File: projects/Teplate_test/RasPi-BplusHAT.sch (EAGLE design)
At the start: 1 part, among them K1 PIN20X2

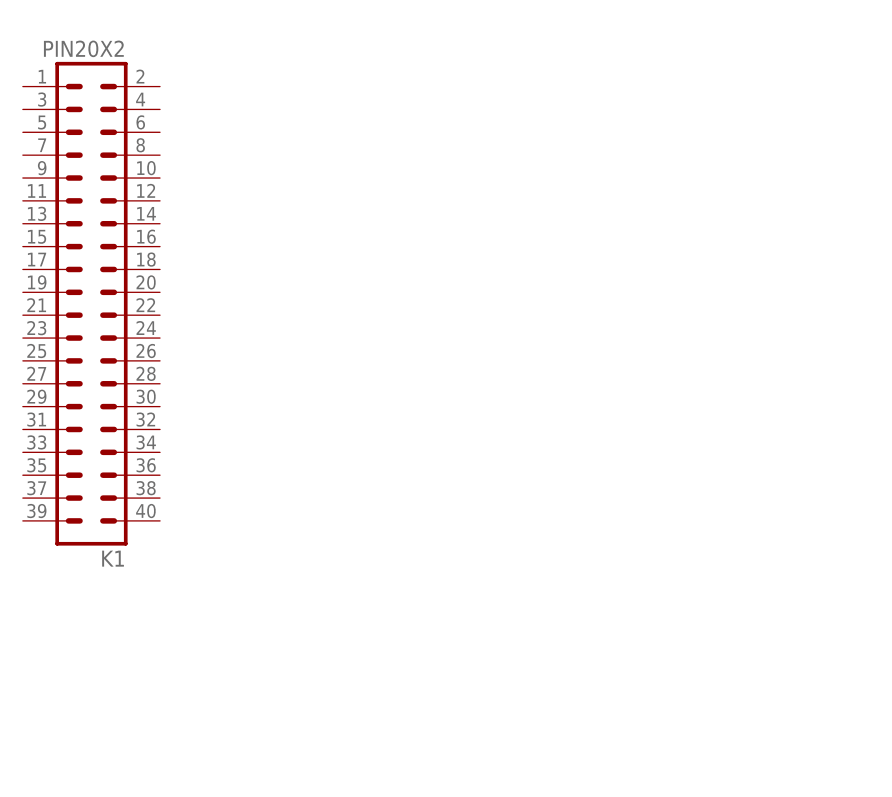
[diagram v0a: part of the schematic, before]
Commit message: Changed Template to be useful
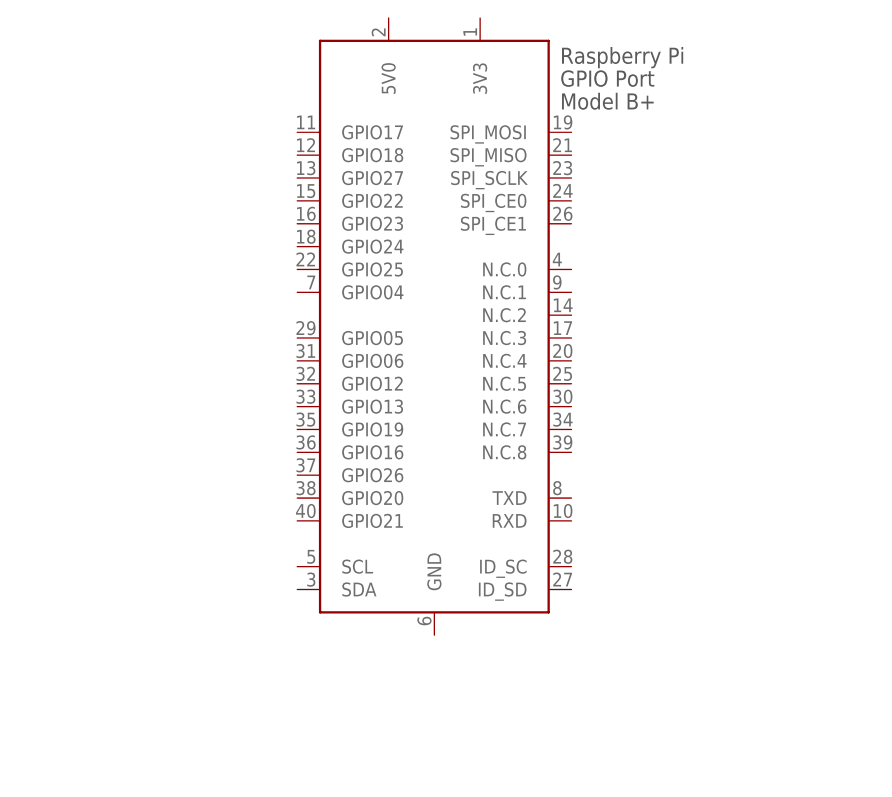
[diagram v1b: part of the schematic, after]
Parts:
- removed K1: PIN20X2, FLYFISH:PIN20X2
- added X1: RASPI_BOARD_B+_E3, raspberrypi_bastelstube_v13:RASPI_BOARD_B+_E3
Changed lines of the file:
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@@
 </classes>
 <parts>
-<part name="K1" library="FLYFISH" deviceset="PIN20X2" device=""/>
 <part name="FRAME1" library="frames" deviceset="A3L-LOC" device=""/>
+<part name="X1" library="raspberrypi_bastelstube_v13" deviceset="RASPI_BOARD_B+" device="_E3"/>
 </parts>
 <sheets>
@@
 </plain>
 <instances>
-<instance part="K1" gate="G$1" x="50.8" y="152.4" smashed="yes" rot="R180">
-<attribute name="VALUE" x="54.61" y="180.34" size="1.778" layer="96" rot="R180"/>
-<attribute name="NAME" x="54.61" y="123.698" size="1.778" layer="95" rot="R180"/>
-</instance>
 <instance part="FRAME1" gate="G$1" x="0" y="0" smashed="yes">
 <attribute name="DRAWING_NAME" x="344.17" y="15.24" size="2.54" layer="94"/>
@@
 <attribute name="SHEET" x="357.505" y="5.08" size="2.54" layer="94"/>
 </instance>
+<instance part="X1" gate="G$1" x="88.9" y="154.94" smashed="yes"/>
 </instances>
 <busses>
